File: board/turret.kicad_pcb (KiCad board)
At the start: 2 copper layers, 57.1 x 38.7 mm, 48 parts, among them M1 SRV_LAS, M2 SRV_SEN, Q1 BC547, U1 STM32F103CBTx, U2 W25Q32JVSS, U3 TPA2005D1DGN, U4 TPS61322xADBV, U5 TLV70028_SOT23-5

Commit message: Partial routing
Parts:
- added H4: MountingHole_Pad, MountingHole:MountingHole_2.2mm_M2_ISO7380_Pad, F.Cu at (131.6, 105.2)
- C1, C10, C11, C12, C13, C14, C15, C16, C18, C19, C2, C3, C4, C5, C6, C8, C9: footprint Capacitor_SMD:C_0603_1608Metric -> Capacitor_SMD:C_0402_1005Metric
- C7: footprint Capacitor_SMD:C_0603_1608Metric -> Capacitor_SMD:C_0402_1005Metric; moved to F.Cu
- D2: footprint Diode_SMD:D_SMA -> Diode_SMD:D_SOD-323
- L1: footprint Inductor_THT:L_Axial_L7.0mm_D3.3mm_P10.16mm_Horizontal_Fastron_MICC -> Inductor_SMD:L_1008_2520Metric
- Q1: value BC547 -> BC848; footprint Package_TO_SOT_THT:TO-92_Inline_Wide -> Package_TO_SOT_SMD:SOT-23
- R1, R3, R4, R5, R6, R7, R8: footprint Resistor_SMD:R_0603_1608Metric -> Resistor_SMD:R_0402_1005Metric
- R2: footprint Resistor_SMD:R_0603_1608Metric -> Resistor_SMD:R_0402_1005Metric; moved to F.Cu
- U2: value W25Q32JVSS -> W25Q16JLSSIG; footprint Package_DIP:DIP-8_W7.62mm -> Package_SO:SOIC-8_5.23x5.23mm_P1.27mm
- moved H3 197.6 mm to (243.8, 147.3)
- moved M2 144.0 mm to (239.4, 106.7), turned to 0 degrees
- moved H2 142.3 mm to (243.8, 64.1)
- moved R8 139.8 mm to (224.0, 112.3), turned to 0 degrees
- moved M1 139.4 mm to (239.4, 97.2), turned to 0 degrees
- moved LD1 139.3 mm to (236.2, 117.5), turned to 0 degrees
- moved BT1 136.3 mm to (236.2, 78.1), turned to 0 degrees
- moved Q1 134.1 mm to (227.3, 114.9), turned to 0 degrees
- moved C17 130.8 mm to (221.0, 74.3), turned to 0 degrees
- moved R7 117.6 mm to (199.6, 115.8), turned to 270 degrees
- moved D2 117.2 mm to (200.6, 113.8)
- moved C13 116.3 mm to (200.7, 108.2)
- moved C14 116.0 mm to (198.1, 108.2), turned to 0 degrees
- moved C18 115.6 mm to (201.2, 115.3)
- moved L1 115.6 mm to (197.1, 110.7)
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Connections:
- Q1 pad 1: Net-(LD1-Pad1) -> Net-(Q1-Pad1)
- Q1 pad 2: Net-(Q1-Pad2) -> GNDA
- Q1 pad 3: GNDA -> Net-(LD1-Pad1)
- R8 pad 1: Net-(Q1-Pad2) -> Net-(Q1-Pad1)
- U1 pad 10: Net-(U1-Pad10) -> (no net)
- U1 pad 16: Net-(U1-Pad16) -> (no net)
- U1 pad 17: Net-(U1-Pad17) -> (no net)
- U1 pad 19: Net-(U1-Pad19) -> (no net)
- U1 pad 2: Net-(U1-Pad2) -> (no net)
- U1 pad 20: Net-(U1-Pad20) -> (no net)
- U1 pad 21: Net-(U1-Pad21) -> (no net)
- U1 pad 22: Net-(U1-Pad22) -> (no net)
- U1 pad 3: Net-(U1-Pad3) -> (no net)
- U1 pad 31: Net-(U1-Pad31) -> (no net)
- U1 pad 32: Net-(U1-Pad32) -> (no net)
- U1 pad 33: Net-(U1-Pad33) -> (no net)
- U1 pad 38: Net-(U1-Pad38) -> (no net)
- U1 pad 4: Net-(U1-Pad4) -> (no net)
- U1 pad 40: Net-(U1-Pad40) -> (no net)
- U1 pad 41: Net-(U1-Pad41) -> (no net)
- U1 pad 44: Net-(U1-Pad44) -> (no net)
- U1 pad 45: Net-(U1-Pad45) -> (no net)
- U1 pad 46: Net-(U1-Pad46) -> (no net)
- U1 pad 5: Net-(U1-Pad5) -> (no net)
- U1 pad 6: Net-(U1-Pad6) -> (no net)
- U3 pad 2: Net-(U3-Pad2) -> (no net)
- U3 pad 9: GNDA -> (no net)
- U5 pad 4: GNDA -> (no net)
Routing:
- net GNDA: track 102.7 -> 0.00 mm, vias 14 -> 0
- net VDD: track 92.2 -> 0.00 mm, vias 5 -> 0
- net +5V: track 78.8 -> 0.00 mm, vias 2 -> 0
- net /SRV_LAS: track 69.0 -> 0.00 mm
- net /SRV_SEN: track 58.6 -> 0.00 mm
- net Net-(BT1-Pad1): track 42.3 -> 0.00 mm, vias 3 -> 0
- net /LASER: track 32.6 -> 0.00 mm
- net /SER_TX: track 30.2 -> 0.00 mm
- net /SER_RX: track 27.9 -> 0.00 mm
- net /SPI_SCK: track 24.9 -> 0.00 mm
- net /SWCLK: track 23.4 -> 0.00 mm, vias 1 -> 0
- net /SWDIO: track 20.9 -> 0.00 mm, vias 1 -> 0
- net /AU_ENAB: track 14.2 -> 0.00 mm
- net Net-(C8-Pad1): track 13.9 -> 0.00 mm, vias 2 -> 0
- net /SPI_MOSI: track 13.6 -> 0.00 mm
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- removed copper zone on B.Cu, net GNDA
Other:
- board outline removed

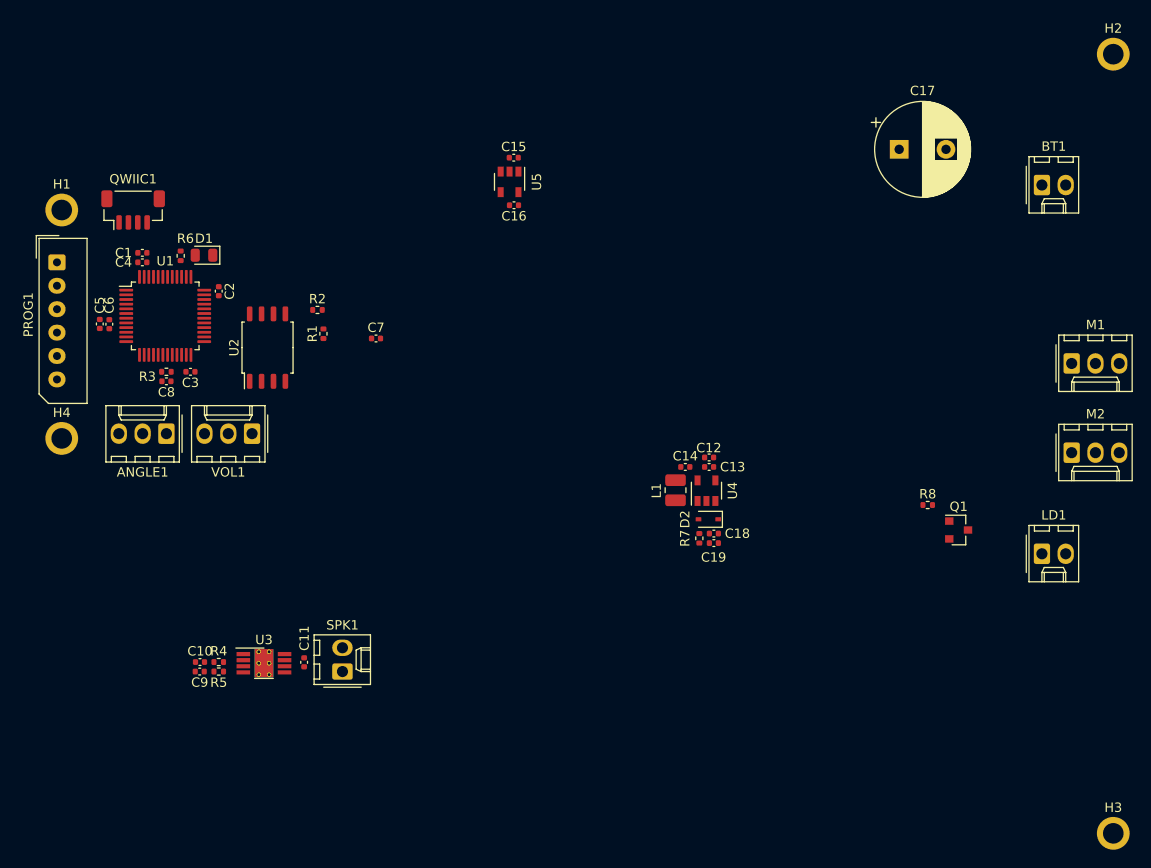
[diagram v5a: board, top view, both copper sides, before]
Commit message: Add tooling holes
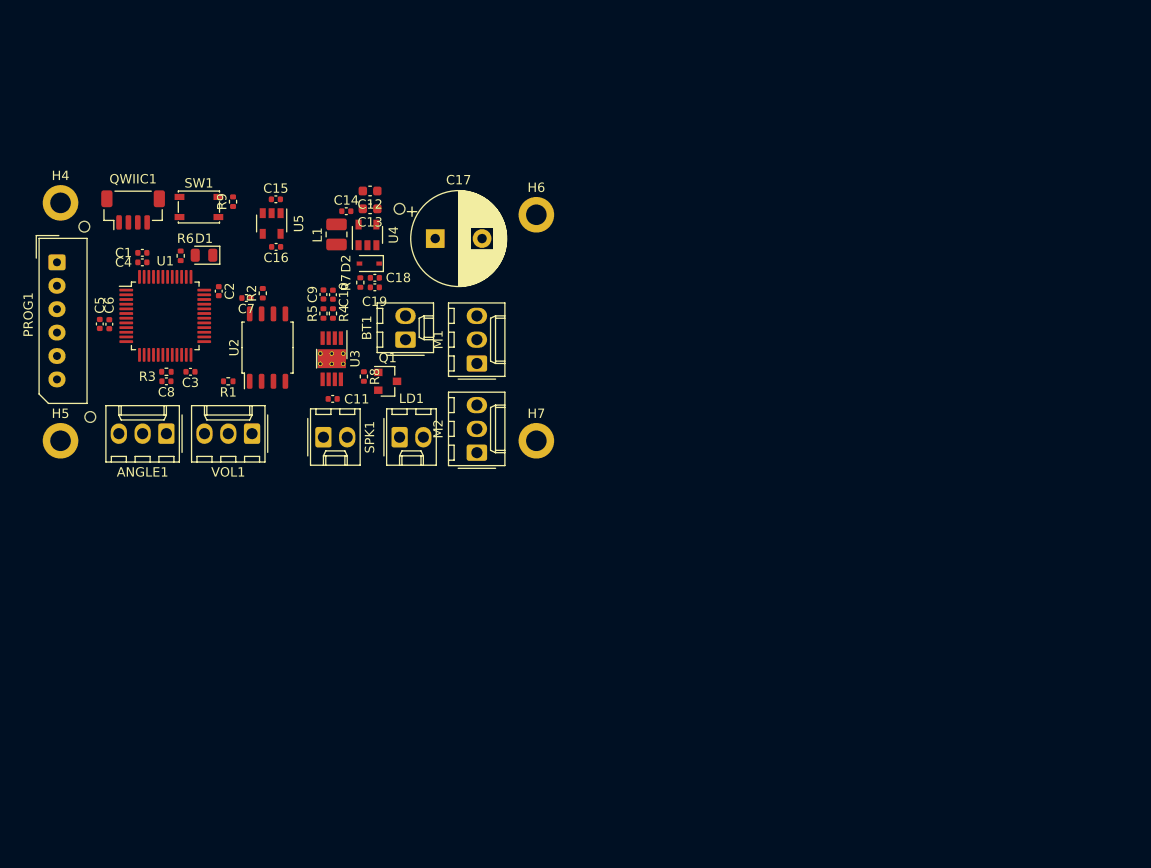
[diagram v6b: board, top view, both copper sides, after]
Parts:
- added H5: MountingHole_Pad, MountingHole:MountingHole_2.2mm_M2_DIN965_Pad, F.Cu at (131.4, 105.4)
- added H6: MountingHole_Pad, MountingHole:MountingHole_2.2mm_M2_DIN965_Pad, F.Cu at (182.2, 81.3)
- added H7: MountingHole_Pad, MountingHole:MountingHole_2.2mm_M2_DIN965_Pad, F.Cu at (182.2, 105.4)
- added R9: 10K, Resistor_SMD:R_0402_1005Metric, F.Cu at (149.9, 79.9)
- added SW1: SW_Push, Button_Switch_SMD:SW_SPST_PTS810, F.Cu at (146.2, 80.5)
- C12, C13: footprint Capacitor_SMD:C_0402_1005Metric -> Capacitor_SMD:C_0603_1608Metric
- H1, H2, H3: value MountingHole_Pad -> MountingHole; footprint MountingHole:MountingHole_2.2mm_M2_ISO7380_Pad -> Custom_IC:JLCPCB_Tooling_Hole
- H4: footprint MountingHole:MountingHole_2.2mm_M2_ISO7380_Pad -> MountingHole:MountingHole_2.2mm_M2_DIN965_Pad
- moved H2 115.9 mm to (134.6, 102.9)
- moved H3 101.3 mm to (167.6, 80.6)
- moved BT1 69.9 mm to (168.3, 94.6), turned to 90 degrees
- moved LD1 69.7 mm to (167.6, 105.0)
- moved M1 63.5 mm to (175.9, 97.2), turned to 90 degrees
- moved M2 63.5 mm to (175.9, 106.7), turned to 90 degrees
- moved Q1 63.0 mm to (166.4, 99.1)
- moved R8 61.7 mm to (163.8, 98.5), turned to 270 degrees
- moved C17 50.4 mm to (171.4, 83.8)
- moved C12 46.0 mm to (164.5, 78.7)
- moved C13 45.5 mm to (164.5, 80.6)
- moved L1 45.3 mm to (160.9, 83.4)
- moved C18 45.3 mm to (165.0, 88.0)
- moved D2 45.3 mm to (164.4, 86.5)
- moved R7 45.3 mm to (163.4, 88.5)
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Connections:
- H4 pad 1: GNDA -> GND
- U1 pad 41: (no net) -> /BUTTON
- U4 pad 3: +5V -> (no net)
- U4 pad 5: GNDA -> (no net)

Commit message: Update to kicad 6
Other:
- net class Default removed
- net class PWR removed

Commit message: Board layout complete
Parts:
- removed H5, H6, H7: MountingHole_Pad, MountingHole:MountingHole_2.2mm_M2_DIN965_Pad
- moved H4 24.7 mm to (154.0, 90.0)
- moved H2 21.8 mm to (156.0, 107.0)
- moved BT1 13.7 mm to (177.0, 84.0)
- moved ANGLE1 13.3 mm to (129.5, 105.0), turned to 0 degrees
- moved C12 12.3 mm to (172.3, 88.2)
- moved C13 12.3 mm to (172.3, 90.1)
- moved L1 12.3 mm to (168.7, 92.8)
- moved C14 12.3 mm to (169.7, 90.4)
- moved C18 12.3 mm to (172.8, 97.5)
- moved C19 12.3 mm to (172.8, 98.5)
- moved D2 12.3 mm to (172.2, 96.0)
- moved R7 12.3 mm to (171.2, 98.0)
- moved U4 12.3 mm to (172.0, 92.9)
- moved VOL1 11.9 mm to (140.0, 105.0), turned to 0 degrees
- moved C17 6.56 mm to (165.0, 85.0), turned to 90 degrees
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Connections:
- H4 pad 1: GND -> GNDA
- U1 pad 10: (no net) -> unconnected-(U1-Pad10)
- U1 pad 16: (no net) -> unconnected-(U1-Pad16)
- U1 pad 17: (no net) -> unconnected-(U1-Pad17)
- U1 pad 19: (no net) -> unconnected-(U1-Pad19)
- U1 pad 2: (no net) -> unconnected-(U1-Pad2)
- U1 pad 20: (no net) -> unconnected-(U1-Pad20)
- U1 pad 21: (no net) -> unconnected-(U1-Pad21)
- U1 pad 22: (no net) -> unconnected-(U1-Pad22)
- U1 pad 3: (no net) -> unconnected-(U1-Pad3)
- U1 pad 31: (no net) -> unconnected-(U1-Pad31)
- U1 pad 32: (no net) -> unconnected-(U1-Pad32)
- U1 pad 33: (no net) -> unconnected-(U1-Pad33)
- U1 pad 38: (no net) -> unconnected-(U1-Pad38)
- U1 pad 4: (no net) -> unconnected-(U1-Pad4)
- U1 pad 40: (no net) -> unconnected-(U1-Pad40)
- U1 pad 44: (no net) -> unconnected-(U1-Pad44)
- U1 pad 45: (no net) -> unconnected-(U1-Pad45)
- U1 pad 46: (no net) -> unconnected-(U1-Pad46)
- U1 pad 5: (no net) -> unconnected-(U1-Pad5)
- U1 pad 6: (no net) -> unconnected-(U1-Pad6)
- U3 pad 2: (no net) -> unconnected-(U3-Pad2)
- U3 pad 9: (no net) -> GNDA
- U4 pad 3: (no net) -> +5V
- U4 pad 5: (no net) -> GNDA
- U5 pad 4: (no net) -> GNDA
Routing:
- net VDD: track 0.00 -> 133.4 mm
- net GNDA: track 0.00 -> 78.8 mm, vias 0 -> 13
- net +5V: track 0.00 -> 55.8 mm
- net /AU_ENAB: track 0.00 -> 51.9 mm, vias 0 -> 4
- net /LASER: track 0.00 -> 50.2 mm, vias 0 -> 4
- net /SRV_SEN: track 0.00 -> 44.9 mm, vias 0 -> 2
- net /SRV_LAS: track 0.00 -> 42.9 mm, vias 0 -> 2
- net Net-(BT1-Pad1): track 0.00 -> 42.5 mm, vias 0 -> 2
- net Net-(C10-Pad1): track 0.00 -> 38.9 mm
- net /SWCLK: track 0.00 -> 21.0 mm, vias 0 -> 1
- net /SWDIO: track 0.00 -> 19.9 mm, vias 0 -> 1
- net /SPI_SCK: track 0.00 -> 16.2 mm
- net Net-(R2-Pad1): track 0.00 -> 14.8 mm
- net /ANGLE_POT: track 0.00 -> 14.4 mm, vias 0 -> 2
- net /SPI_MISO: track 0.00 -> 14.0 mm
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- added copper zone on B.Cu, net GNDA
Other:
- board outline added: 56 x 32 mm
